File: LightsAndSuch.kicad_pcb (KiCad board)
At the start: 2 copper layers, 106.7 x 100 mm, 74 parts, among them J1 Conn_ARM_SWD_TagConnect_TC2030, J2 VIN, J3 TSA, J4 BMS Fault, J5 Button, J6 IMD Fault, J7 Break, Q1 AO3400A, Q2 AO3400A, Q3 AO3400A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

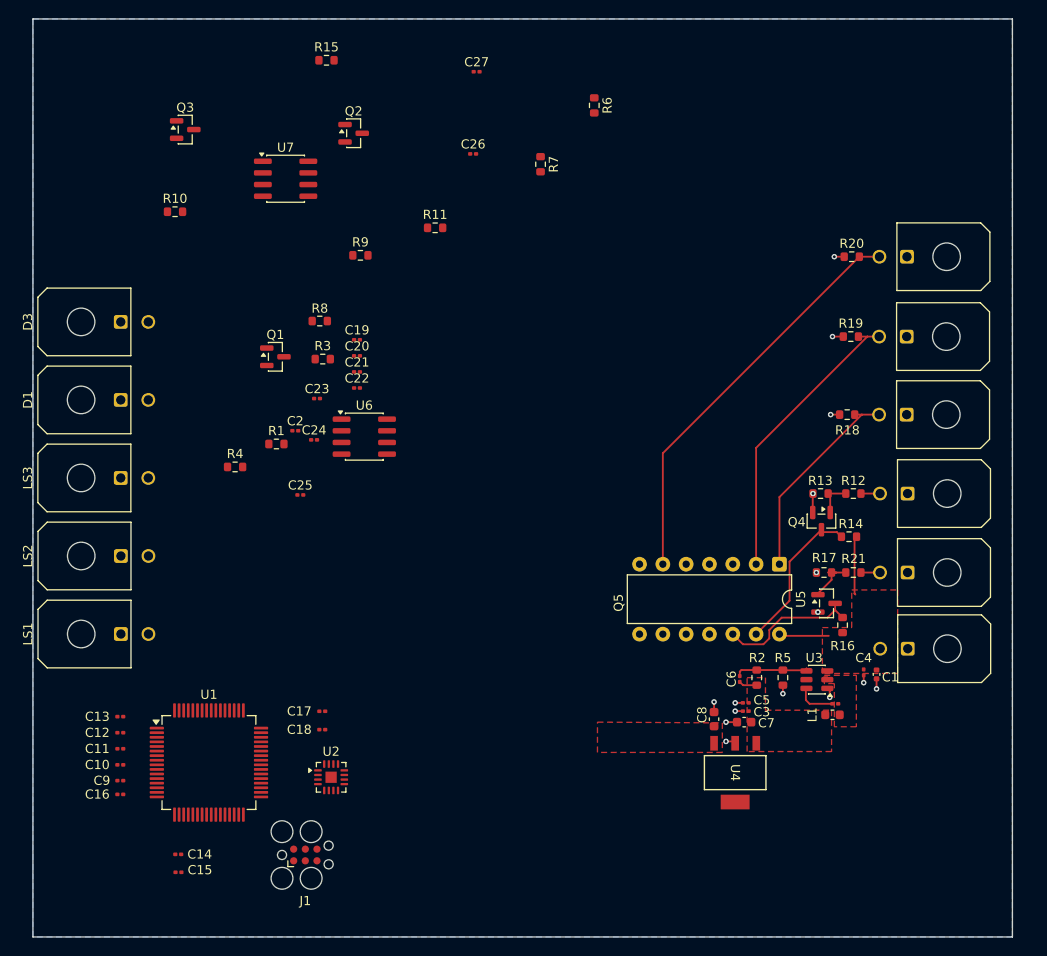
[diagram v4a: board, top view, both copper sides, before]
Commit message: 4 layer + buzzer circuit
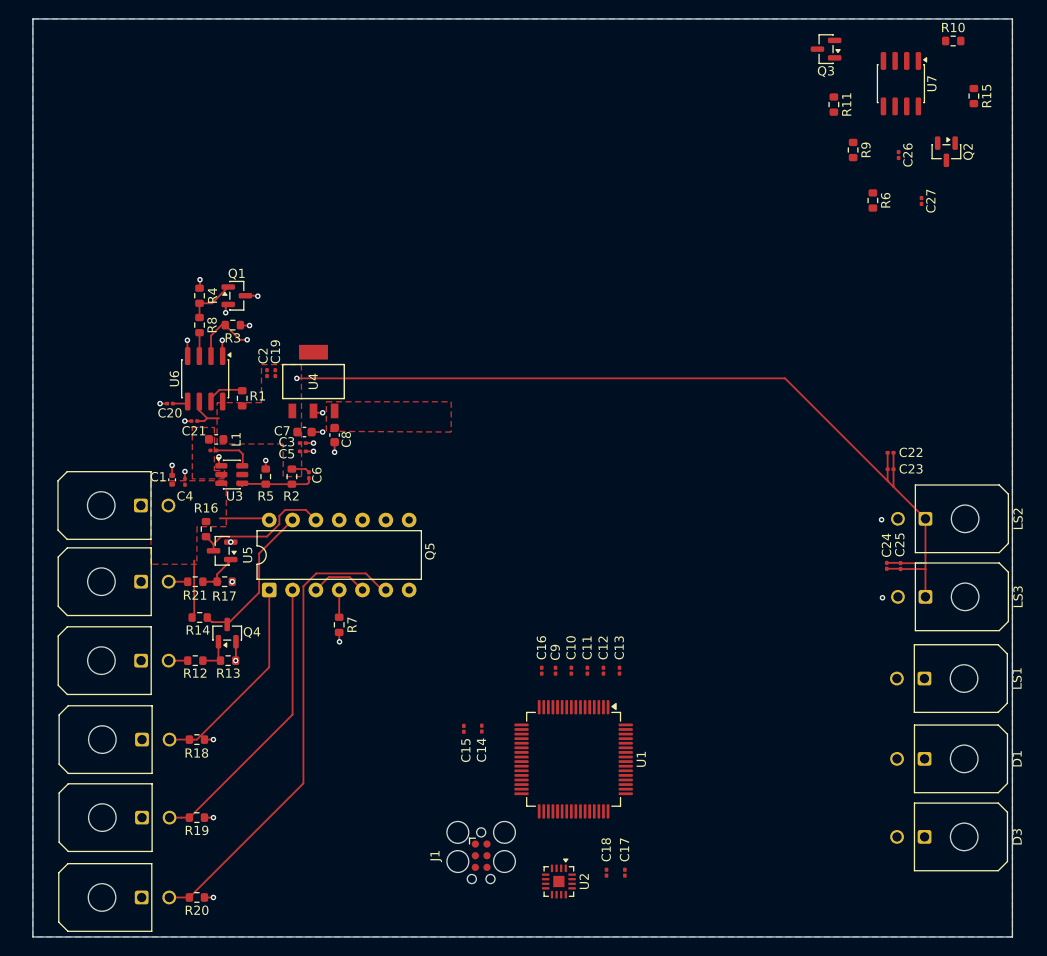
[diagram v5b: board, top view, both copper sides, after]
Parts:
- moved J5 108.7 mm to (69.3, 142.7), turned to 90 degrees
- moved D3 104.0 mm to (154.6, 136.1), turned to -90 degrees
- moved R20 99.8 mm to (75.4, 142.7), turned to 180 degrees
- moved J7 98.4 mm to (69.4, 134.0), turned to 90 degrees
- moved D1 95.9 mm to (154.6, 127.6), turned to -90 degrees
- moved J3 90.5 mm to (69.4, 125.5), turned to 90 degrees
- moved LS3 88.6 mm to (154.7, 110.0), turned to -90 degrees
- moved R19 88.4 mm to (75.4, 134.0), turned to 180 degrees
- moved LS2 87.7 mm to (154.7, 101.5), turned to -90 degrees
- moved LS1 87.7 mm to (154.6, 118.8), turned to -90 degrees
- moved R10 86.8 mm to (157.8, 49.4)
- moved J4 85.5 mm to (69.3, 116.9), turned to 90 degrees
- moved J2 85.0 mm to (69.3, 100.0), turned to 90 degrees
- moved J6 83.5 mm to (69.3, 108.3), turned to 90 degrees
- moved C1 79.6 mm to (72.7, 97.2), turned to 90 degrees
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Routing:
- net +5V: track 2.00 -> 105.4 mm, vias 0 -> 1
- net Net-(Q1-D): track 0.00 -> 91.6 mm, vias 0 -> 3
- net Trigger: track 0.00 -> 70.4 mm, vias 0 -> 2
- net GND: track 14.2 -> 22.1 mm, vias 15 -> 22
- net Button: track 44.6 -> 51.5 mm
- net Net-(U5-C): track 0.00 -> 6.24 mm
- net Net-(Q1-G): track 0.00 -> 5.59 mm
- net Net-(U6-DIS): track 0.00 -> 4.17 mm
- net Net-(U5-K): track 0.00 -> 2.97 mm
- net Net-(U6-Q): track 0.00 -> 2.56 mm
- net Net-(U6-CV): track 0.00 -> 1.70 mm
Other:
- copper layers 2 -> 4

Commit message: rp2040
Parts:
- added C28: C, Capacitor_SMD:C_0201_0603Metric, F.Cu at (137.4, 121.3)
- added C29: C, Capacitor_SMD:C_0201_0603Metric, F.Cu at (137.4, 123.1)
- added C30: C, Capacitor_SMD:C_0201_0603Metric, F.Cu at (137.4, 124.8)
- added C31: 100n, Capacitor_SMD:C_0201_0603Metric, F.Cu at (137.4, 126.6)
- added C32: 10u, Capacitor_SMD:C_0201_0603Metric, F.Cu at (137.4, 128.3)
- added C33: 10u, Capacitor_SMD:C_0201_0603Metric, F.Cu at (137.4, 130.1)
- added P1: USB_C_Plug_USB2.0, Connector_USB:USB_C_Receptacle_Amphenol_124019772112A, F.Cu at (130.1, 125.9)
- added R22: 1k, Resistor_SMD:R_0603_1608Metric, F.Cu at (140.6, 121.7)
- added U8: W25Q128JVS, Package_SO:SOIC-8_5.3x5.3mm_P1.27mm, F.Cu at (129.3, 134.8)
- added U9: NCP1117-3.3_SOT223, Package_TO_SOT_SMD:SOT-223-3_TabPin2, F.Cu at (139.4, 135.5)
- C15: value 1u -> 100n
- C16: value 4.7u' -> 100n
- C9: value 100n -> 1u
- J1: value Conn_ARM_SWD_TagConnect_TC2030 -> Conn_01x02_Pin; footprint Connector:Tag-Connect_TC2030-IDC-FP_2x03_P1.27mm_Vertical -> Connector_PinHeader_2.00mm:PinHeader_1x02_P2.00mm_Vertical
- U1: value STM32F205RBTx -> RP2040; footprint Package_QFP:LQFP-64_10x10mm_P0.5mm -> Package_DFN_QFN:QFN-56-1EP_7x7mm_P0.4mm_EP3.2x3.2mm
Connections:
- C14 pad 1: GND -> +3.3V
- C14 pad 2: +3.3V -> GND
- C15 pad 1: GND -> +3.3V
- C15 pad 2: +3.3V -> GND
- C9 pad 1: +3.3V -> GND
- C9 pad 2: GND -> +3.3V
- J1 pad 1: +3.3V -> GND
- J1 pad 2: Net-(J1-SWDIO) -> Net-(J1-Pin_2)
- U1 pad 10: unconnected-(U1-PC2-Pad10) -> +3.3V
- U1 pad 12: GND -> unconnected-(U1-GPIO9-Pad12)
- U1 pad 13: +3.3V -> Net-(U1-GPIO10)
- U1 pad 14: unconnected-(U1-PA0-Pad14) -> Net-(U1-GPIO11)
- U1 pad 15: unconnected-(U1-PA1-Pad15) -> Net-(U1-GPIO12)
- U1 pad 18: GND -> unconnected-(U1-GPIO15-Pad18)
- U1 pad 19: +3.3V -> unconnected-(U1-TESTEN-Pad19)
- U1 pad 2: unconnected-(U1-PC13-Pad2) -> Trigger
- U1 pad 22: unconnected-(U1-PA6-Pad22) -> +3.3V
- U1 pad 23: unconnected-(U1-PA7-Pad23) -> Net-(U1-VREG_VOUT)
- U1 pad 32: +3.3V -> unconnected-(U1-GPIO21-Pad32)
- U1 pad 33: unconnected-(U1-PB12-Pad33) -> +3.3V
- U1 pad 34: Net-(U1-PB13) -> unconnected-(U1-GPIO22-Pad34)
- U1 pad 36: Net-(U1-PB15) -> unconnected-(U1-GPIO24-Pad36)
- U1 pad 42: unconnected-(U1-PA9-Pad42) -> +3.3V
- U1 pad 43: unconnected-(U1-PA10-Pad43) -> +3.3V
- U1 pad 44: unconnected-(U1-PA11-Pad44) -> +3.3V
- U1 pad 45: unconnected-(U1-PA12-Pad45) -> Net-(U1-VREG_VOUT)
- U1 pad 46: Net-(J1-SWDIO) -> /USB_D-
- U1 pad 47: unconnected-(U1-VCAP_2-Pad47) -> /USB_D+
- U1 pad 49: Net-(J1-SWCLK) -> +3.3V
- U1 pad 50: unconnected-(U1-PA15-Pad50) -> Net-(U1-VREG_VOUT)
- U1 pad 51: unconnected-(U1-PC10-Pad51) -> /QSPI_SD2
- U1 pad 52: unconnected-(U1-PC11-Pad52) -> /QSPI_SD3
- U1 pad 53: unconnected-(U1-PC12-Pad53) -> /QSPI_SCLK
- U1 pad 54: unconnected-(U1-PD2-Pad54) -> /QSPI_SD1
- U1 pad 55: Net-(J1-SWO) -> /QSPI_SDO
- U1 pad 56: Net-(J1-~{RESET}) -> /QSPI_SS
- U1 pad 57: unconnected-(U1-PB5-Pad57) -> GND
- U1 pad 8: Trigger -> unconnected-(U1-GPIO6-Pad8)
- U2 pad 1: Net-(U1-PB15) -> Net-(U1-GPIO12)
- U2 pad 14: Net-(U1-PB9) -> Net-(U1-GPIO10)
- U2 pad 16: Net-(U1-PB13) -> Net-(U1-GPIO11)

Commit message: rev 1
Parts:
- moved R10 97.0 mm to (111.3, 134.6), turned to 90 degrees
- moved R15 96.9 mm to (99.8, 131.4)
- moved Q2 94.4 mm to (100.4, 137.0)
- moved U7 92.7 mm to (106.3, 134.7)
- moved Q3 86.5 mm to (107.4, 128.7), turned to 90 degrees
- moved R9 85.1 mm to (110.1, 138.0)
- moved C26 84.0 mm to (114.0, 136.8), turned to 90 degrees
- moved R11 83.1 mm to (104.5, 129.0)
- moved C27 80.1 mm to (112.5, 135.1)
- moved R6 68.3 mm to (82.2, 81.1), turned to 90 degrees
- moved J1 65.8 mm to (112.6, 72.7)
- moved U8 61.3 mm to (107.0, 77.7), turned to 180 degrees
- moved R22 59.2 mm to (107.5, 72.7), turned to 180 degrees
- moved C31 59.0 mm to (101.5, 79.7), turned to 180 degrees
- moved U9 55.0 mm to (132.9, 80.8)
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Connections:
- U2 pad 7: +5V -> (no net)
- U2 pad 8: +5V -> (no net)
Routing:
- net +12V: track 11.8 -> 113.3 mm, vias 0 -> 2
- net +3.3V: track 0.00 -> 68.0 mm, vias 0 -> 5
- net Fault: track 0.00 -> 46.6 mm, vias 0 -> 2
- net Net-(D1-K): track 0.00 -> 32.9 mm, vias 0 -> 1
- net GND: track 22.1 -> 53.1 mm, vias 22 -> 57
- net Net-(U2-OUTP): track 0.00 -> 25.6 mm
- net /USB_D+: track 0.00 -> 24.6 mm, vias 0 -> 2
- net /USB_D-: track 0.00 -> 24.1 mm, vias 0 -> 2
- net Net-(U2-OUTN): track 0.00 -> 21.9 mm
- net /QSPI_SS: track 0.00 -> 18.2 mm, vias 0 -> 2
- net /QSPI_SDO: track 0.00 -> 17.5 mm
- net /QSPI_SCLK: track 0.00 -> 16.1 mm
- net Net-(Q2-S): track 0.00 -> 16.1 mm
- net /QSPI_SD2: track 0.00 -> 14.0 mm, vias 0 -> 2
- net +5V: track 105.4 -> 91.8 mm, vias 1 -> 3
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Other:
- board size 106.7 x 100 mm -> 80.3 x 76.8 mm

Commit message: grounding out and moving some
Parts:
- moved Q2 14.1 mm to (87.0, 141.5)
- moved Q3 14.1 mm to (94.0, 133.2)
- moved C26 14.1 mm to (100.7, 141.4)
- moved C27 14.1 mm to (99.1, 139.7)
- moved R10 14.1 mm to (97.9, 139.1)
- moved R15 14.1 mm to (86.5, 135.9)
- moved U7 14.1 mm to (93.0, 139.3)
- moved R11 14.1 mm to (91.1, 133.6)
- moved R9 14.1 mm to (96.7, 142.6)
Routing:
- net Trigger: track 71.7 -> 95.4 mm
- net Net-(D1-K): track 32.9 -> 54.1 mm
- net +5V: track 91.8 -> 107.9 mm, vias 3 -> 4
- net +12V: track 113.3 -> 124.0 mm
- net +3.3V: track 68.0 -> 72.3 mm
- net Fault: track 46.6 -> 49.5 mm
- added copper zone on In1.Cu, net GND
- added copper zone on In2.Cu, net GND
